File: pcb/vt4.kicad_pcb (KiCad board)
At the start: 2 copper layers, 160 x 60 mm, 35 parts, among them J1 DE9, J2 DE9, J3 DE9, J4 DE9, J5 Mini-DIN-6, J7 USB_A, J8 USB_C_PowerOnly_6P, Q1 BSS138, Q2 BSS138, SW1 SW_SPDT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

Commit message: Add name and order pcb
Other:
- board text added: "2026-01-14"
- board text added: "Video Terminal 4"
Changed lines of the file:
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@@
 		(layer "Edge.Cuts")
+	)
+	(gr_text "2026-01-14"
+		(at 170.5 67 0)
+		(layer "F.SilkS")
+		(effects
+			(font
+				(size 1 1)
+				(thickness 0.125)
+			)
+			(justify left bottom)
+		)
+	)
+	(gr_text "Video Terminal 4"
+		(at 170 65 0)
+		(layer "F.SilkS")
+		(effects
+			(font
+				(size 2 2)
+				(thickness 0.2)
+			)
+			(justify left bottom)
+		)
 	)
 	(segment

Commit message: PCB fail - connected UART 1 up to HDMI clk pins
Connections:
- U1 pad 19: unconnected-(U1-PIN54-Pad19) -> UART 2 RX
- U1 pad 20: unconnected-(U1-PIN55-Pad20) -> UART 2 TX
- U1 pad 21: UART 2 RX -> UART 1 TX
- U1 pad 22: UART 2 TX -> UART 1 RX
- U1 pad 23: UART 1 TX -> HDMI CLK -
- U1 pad 24: UART 1 RX -> HDMI CLK +
- U1 pad 32: unconnected-(U1-PIN70-Pad32) -> HDMI B -
- U1 pad 33: unconnected-(U1-PIN71-Pad33) -> HDMI B +
- U1 pad 34: unconnected-(U1-PIN72-Pad34) -> HDMI G -
- U1 pad 35: unconnected-(U1-PIN73-Pad35) -> HDMI G +
- U1 pad 36: unconnected-(U1-PIN74-Pad36) -> HDMI R -
- U1 pad 37: unconnected-(U1-PIN75-Pad37) -> HDMI R +
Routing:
- net unconnected-(J2-PAD-Pad0)_1: track 25.0 -> 0.00 mm
- net unconnected-(J2-PAD-Pad0): track 0.00 -> 25.0 mm
- net UART 2 RX: track 21.2 -> 26.3 mm
- net UART 2 TX: track 17.9 -> 22.4 mm
- net UART 1 TX: track 16.0 -> 19.3 mm
- net UART 1 RX: track 13.3 -> 15.4 mm
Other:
- board text added: "2026-01-XX"
- board text removed: "2026-01-14"

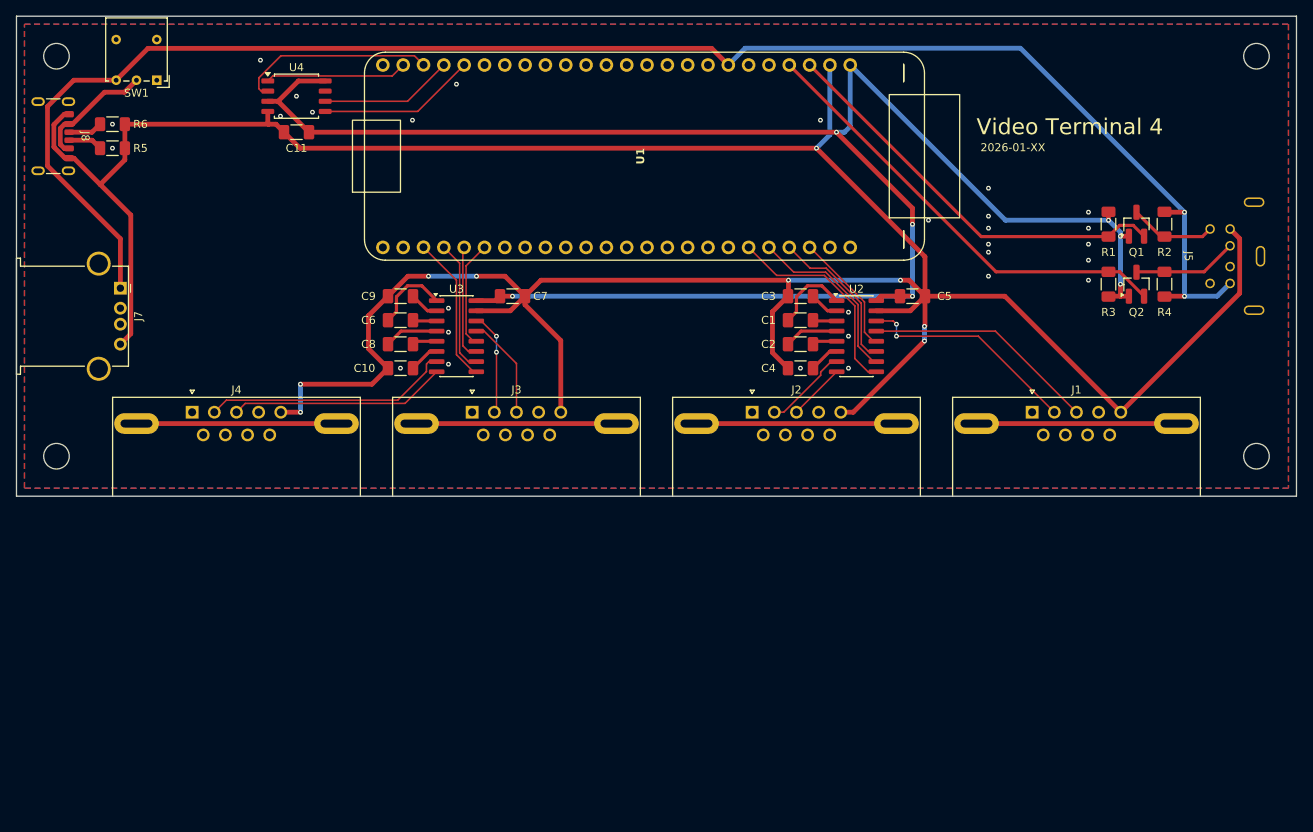
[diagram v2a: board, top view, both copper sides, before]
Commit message: Update PCB based on what was learnt soldering & testing
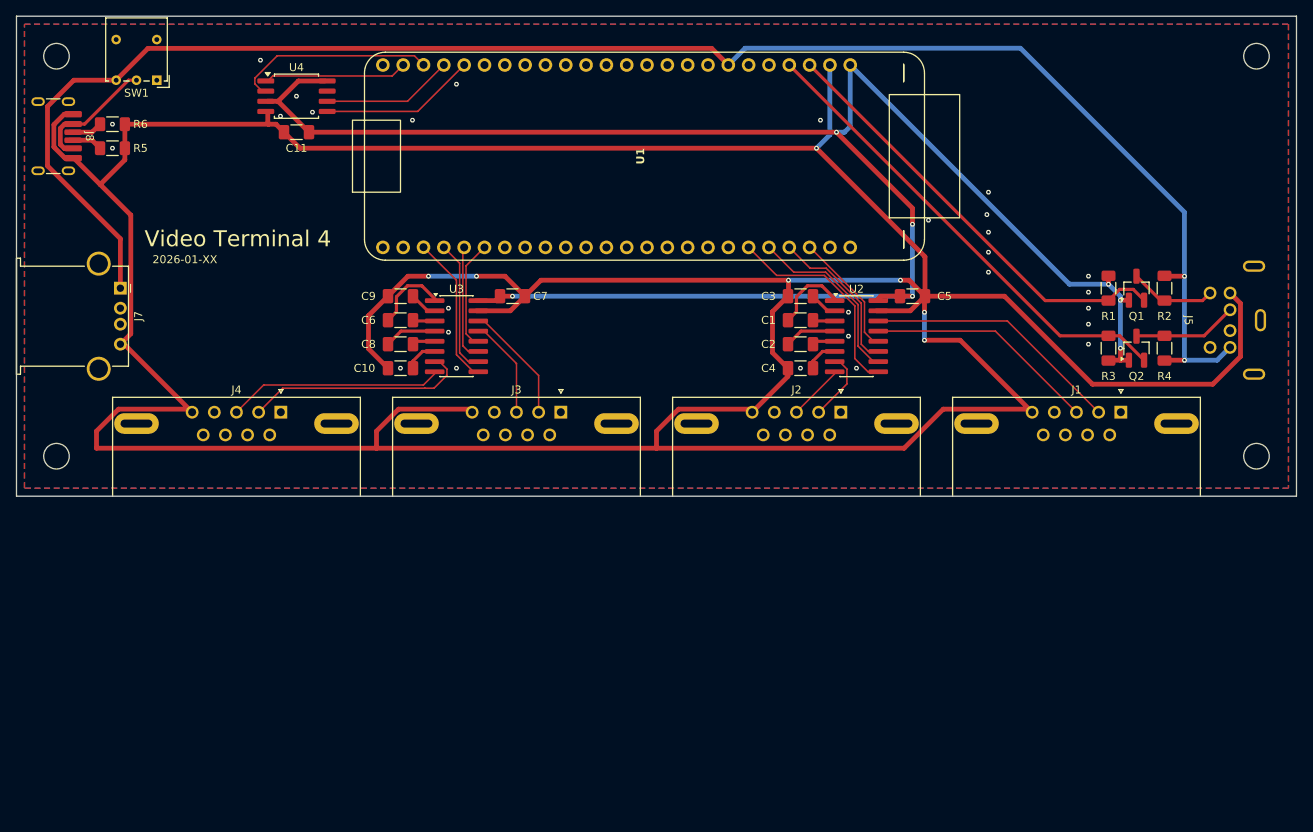
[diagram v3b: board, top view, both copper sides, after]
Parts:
- J1, J2, J3, J4: footprint 0-footprints:DSUB-9_Pins_Horizontal -> 0-footprints:DSUB_9_Pins_Female_Horizontal
- J8: footprint Connector_USB:USB_C_Receptacle_GCT_USB4125-xx-x-0190_6P_TopMnt_Horizontal -> 0-footprints:USB_C_Receptacle_GCT_USB4125-xx-x-0190_6P_TopMnt_Horizontal_Handsolder
- U2, U3: footprint Package_SO:SOIC-16_3.9x9.9mm_P1.27mm -> 0-footprints:SOIC-16_3.9x9.9mm_P1.27mm_Handsolder
- U4: footprint Package_SO:SOIC-8_5.3x5.3mm_P1.27mm -> 0-footprints:SOIC-8_5.3x5.3mm_P1.27mm_Handsolder
- moved J5 8.00 mm to (210.2, 88.0)
- moved Q1 8.00 mm to (190.0, 84.0)
- moved Q2 8.00 mm to (190.0, 91.5)
- moved R1 8.00 mm to (186.5, 84.0)
- moved R2 8.00 mm to (193.5, 84.0)
- moved R3 8.00 mm to (186.5, 91.5)
- moved R4 8.00 mm to (193.5, 91.5)
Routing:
- net GND: track 390.5 -> 538.5 mm, vias 38 -> 35
- net unconnected-(J4-PAD-Pad0)_1: track 25.0 -> 0.00 mm
- net unconnected-(J3-PAD-Pad0)_1: track 25.0 -> 0.00 mm
- net unconnected-(J2-PAD-Pad0) (its old number): track 25.0 -> 0.00 mm
- net unconnected-(J1-PAD-Pad0): track 25.0 -> 0.00 mm
- net +5V: track 203.7 -> 211.7 mm
- net Net-(U2-T1OUT): track 27.9 -> 32.5 mm, vias 2 -> 0
- net +3V3: track 228.4 -> 231.7 mm
- net PS/2 data 3V3: track 56.3 -> 59.6 mm
- net PS/2 clk 3V3: track 51.8 -> 55.1 mm
- net Net-(U3-T2OUT): track 31.0 -> 27.9 mm
- net Net-(U3-T1OUT): track 12.9 -> 15.2 mm, vias 2 -> 0
- net Net-(U2-T2OUT): track 10.7 -> 9.22 mm
- net FeRAM SO: track 24.8 -> 26.0 mm
- net Net-(U3-VS-): track 3.83 -> 4.97 mm
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
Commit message: Send PCB of for manufacturing  * switch FeRAM to 3V3 pins (and supply)  * update FPGA pin numbers to match
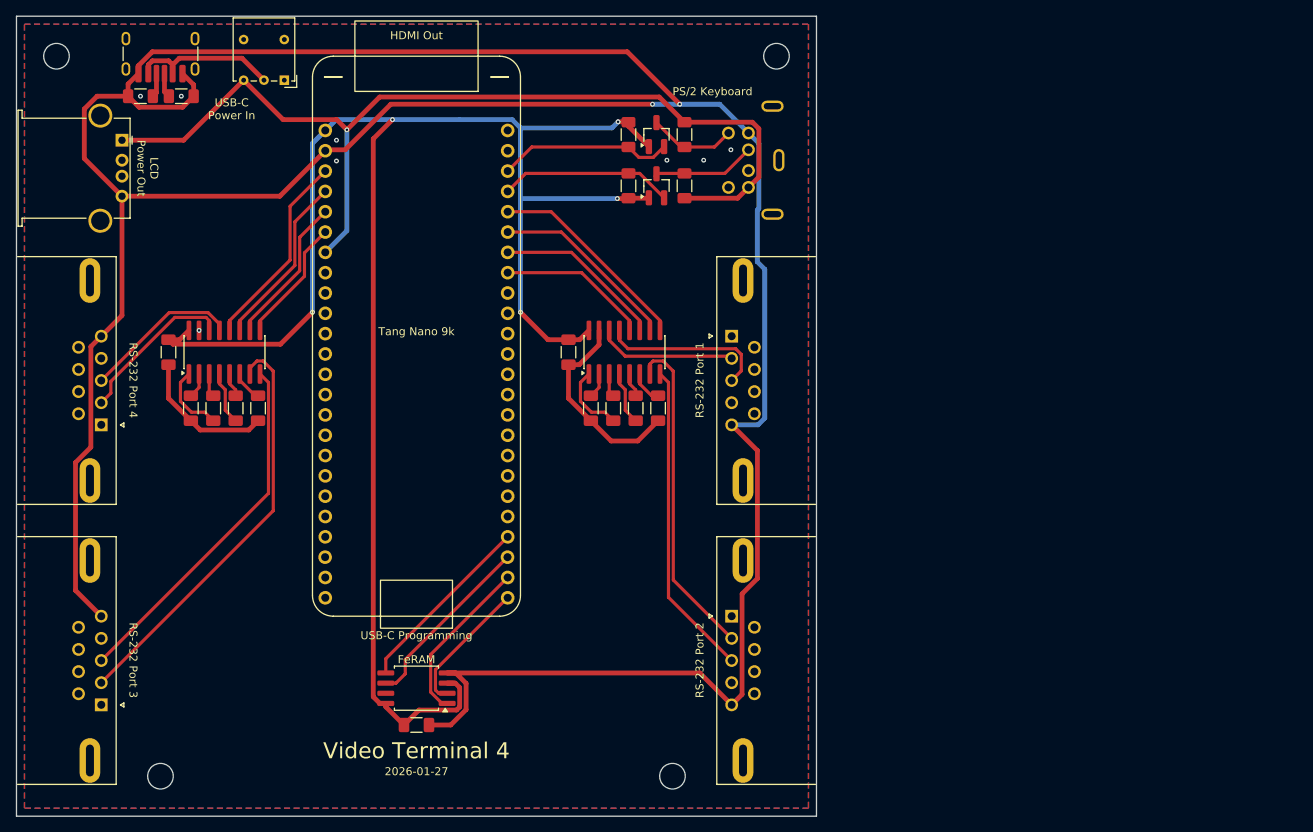
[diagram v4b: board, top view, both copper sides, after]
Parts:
- moved H4 83.2 mm to (132.0, 145.0)
- moved C11 75.6 mm to (100.0, 138.6), turned to 180 degrees
- moved U4 75.5 mm to (100.0, 134.0), turned to 180 degrees
- moved J5 63.4 mm to (150.0, 68.0)
- moved Q2 63.3 mm to (130.0, 71.2)
- moved R3 63.3 mm to (126.5, 71.2)
- moved R4 63.3 mm to (133.5, 71.2)
- moved Q1 63.0 mm to (130.0, 64.8)
- moved R1 63.0 mm to (126.5, 64.8)
- moved R2 63.0 mm to (133.5, 64.8)
- moved H2 60.0 mm to (145.0, 55.0)
- moved U1 55.4 mm to (100.0, 122.7), turned to 180 degrees
- moved J3 52.9 mm to (60.6, 125.0), turned to -90 degrees
- moved C5 43.6 mm to (119.0, 92.0), turned to 90 degrees
- moved C7 43.6 mm to (69.0, 92.0), turned to 90 degrees
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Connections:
- J3 pad 2: Net-(U3-T1OUT) -> Net-(U3-T2OUT)
- J3 pad 3: Net-(U3-R1IN) -> Net-(U3-R2IN)
- J4 pad 2: Net-(U3-T2OUT) -> Net-(U3-T1OUT)
- J4 pad 3: Net-(U3-R2IN) -> Net-(U3-R1IN)
- U1 pad 1: unconnected-(U1-PIN38-Pad1) -> FeRAM SO
- U1 pad 17: unconnected-(U1-PIN51-Pad17) -> UART 1 RX
- U1 pad 18: unconnected-(U1-PIN53-Pad18) -> UART 1 TX
- U1 pad 19: UART 2 RX -> UART 2 TX
- U1 pad 2: unconnected-(U1-PIN37-Pad2) -> FeRAM CS
- U1 pad 20: UART 2 TX -> UART 2 RX
- U1 pad 21: UART 1 TX -> PS/2 data 3V3
- U1 pad 22: UART 1 RX -> PS/2 clk 3V3
- U1 pad 27: PS/2 clk 3V3 -> UART 3 RX
- U1 pad 28: PS/2 data 3V3 -> UART 3 TX
- U1 pad 29: unconnected-(U1-PIN49-Pad29) -> UART 4 TX
- U1 pad 3: UART 4 RX -> FeRAM SCLK
- U1 pad 30: unconnected-(U1-PIN48-Pad30) -> UART 4 RX
- U1 pad 4: UART 4 TX -> FeRAM SI
- U1 pad 44: FeRAM SI -> unconnected-(U1-(1V8)_PIN83-Pad44)
- U1 pad 45: FeRAM SCLK -> unconnected-(U1-(1V8)_PIN84-Pad45)
- U1 pad 46: FeRAM SO -> unconnected-(U1-(1V8)_PIN85-Pad46)
- U1 pad 47: FeRAM CS -> unconnected-(U1-(1V8)_PIN86-Pad47)
- U1 pad 5: UART 3 TX -> unconnected-(U1-PIN25-Pad5)
- U1 pad 6: UART 3 RX -> unconnected-(U1-PIN26-Pad6)
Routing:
- net GND: track 538.5 -> 418.5 mm, vias 35 -> 10
- net +5V: track 211.7 -> 121.6 mm, vias 2 -> 1
- net PS/2 data 3V3: track 59.6 -> 21.7 mm
- net PS/2 clk 3V3: track 55.1 -> 21.9 mm
- net Net-(U2-R2IN): track 7.14 -> 39.5 mm
- net Net-(U2-T2OUT): track 9.22 -> 41.3 mm
- net Net-(U3-T2OUT): track 27.9 -> 52.4 mm
- net Net-(U3-R2IN): track 27.1 -> 44.9 mm
- net Net-(U2-T1OUT): track 32.5 -> 17.5 mm
- net UART 3 RX: track 13.4 -> 24.9 mm
- net FeRAM SO: track 26.0 -> 16.9 mm
- net Net-(U2-R1IN): track 29.2 -> 21.0 mm
- net UART 3 TX: track 14.3 -> 21.8 mm
- net Net-(U3-R1IN): track 12.8 -> 19.7 mm
- net FeRAM SCLK: track 16.7 -> 22.8 mm
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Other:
- board size 160 x 60 mm -> 100 x 100 mm
- board text added: "2026-01-27"
- board text added: "FeRAM"
- board text added: "HDMI Out"
- board text added: "LCD Power Out"
- board text added: "PS/2 Keyboard"
- board text added: "RS-232 Port 1"
- board text added: "RS-232 Port 2"
- board text added: "RS-232 Port 3"
- board text added: "RS-232 Port 4"
- board text added: "Tang Nano 9k"
- board text added: "USB-C Power In"
- board text added: "USB-C Programming"
- board text removed: "2026-01-XX"
